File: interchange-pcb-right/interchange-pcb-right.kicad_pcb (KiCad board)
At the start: 2 copper layers, 158 x 104 mm, 139 parts, among them J1 Conn_01x04, J2 Conn_01x04, J3 TRRS_L, J4 TRRS_R, J5 SSD1306, SW1 RotaryEncoder, U1 Seeeduino Xiao rp2040, U2 PCA9555PW, U3 PCA9555PW, U4 ADS1110, U5 SN74AHCT125PWR, U6 TCA4307DGKR

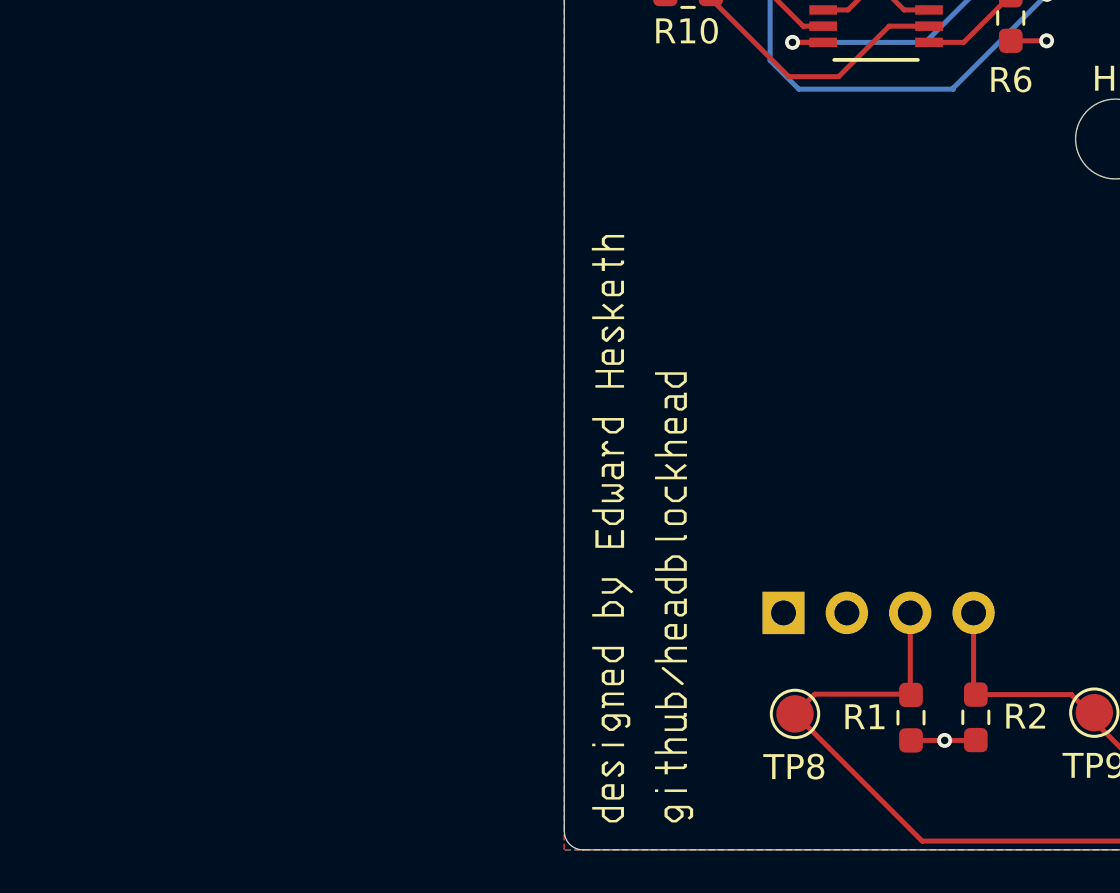
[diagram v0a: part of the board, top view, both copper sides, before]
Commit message: feat: rename right to interchange
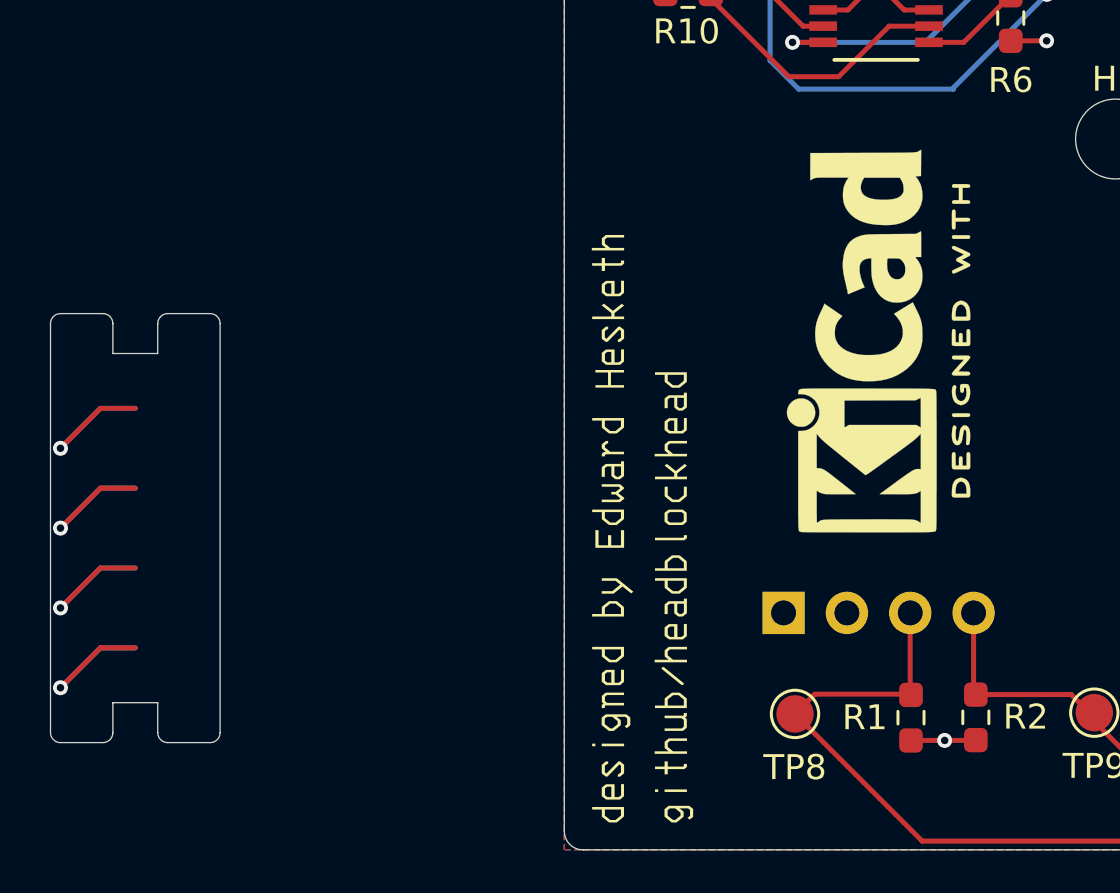
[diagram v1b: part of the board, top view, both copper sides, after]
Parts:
- added REF**: KiCad-Logo2_6mm_SilkScreen, Symbol:KiCad-Logo2_6mm_SilkScreen, F.Cu at (81.9, 129.6)
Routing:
- net (no net): track 0.00 -> 29.3 mm, vias 0 -> 4
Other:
- board size 158 x 104 mm -> 178.6 x 104 mm

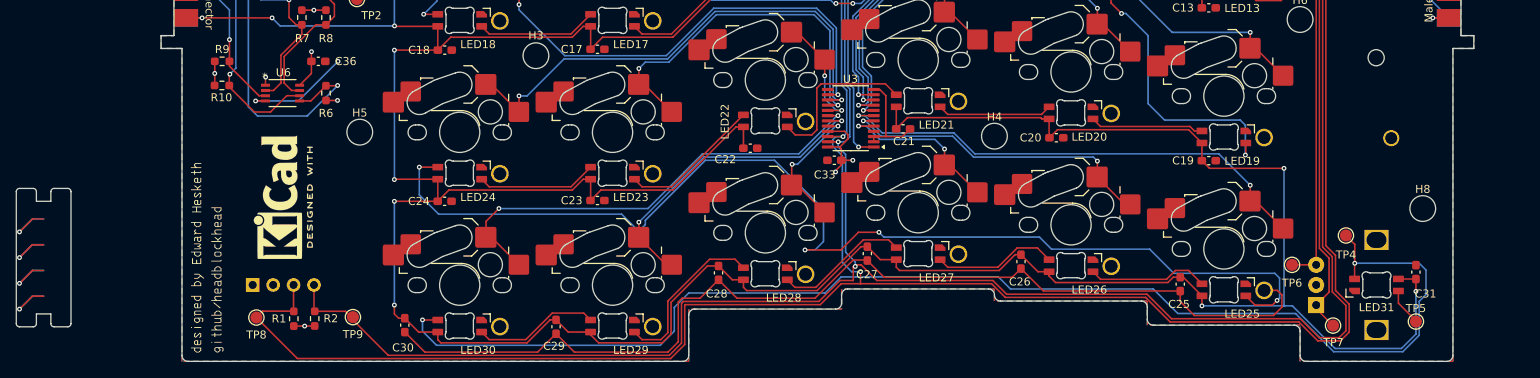
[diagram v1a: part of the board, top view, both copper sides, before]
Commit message: feat: add connectors to pcb-right using snap-off mousebites
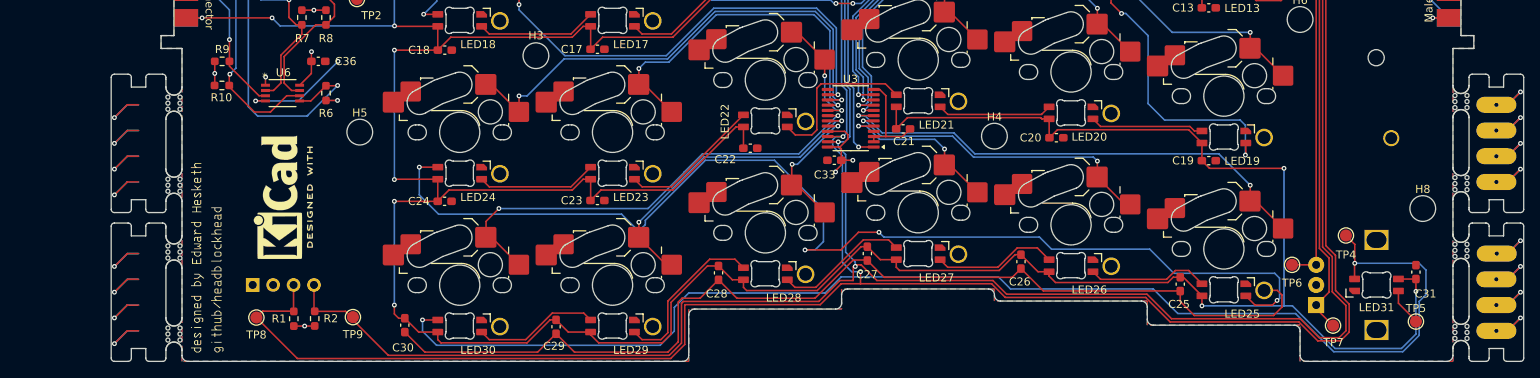
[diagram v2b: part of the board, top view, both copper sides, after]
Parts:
- added REF**: Pogo-0906-0-15-20-76-14-11-0, CustomFootprints:Pogo-0906-0-15-20-76-14-11-0, F.Cu at (233.4, 143.0)
- added REF**: Pogo-0906-0-15-20-76-14-11-0, CustomFootprints:Pogo-0906-0-15-20-76-14-11-0, F.Cu at (233.4, 146.2)
- added REF**: Pogo-0906-0-15-20-76-14-11-0, CustomFootprints:Pogo-0906-0-15-20-76-14-11-0, F.Cu at (233.4, 127.7)
- added REF**: Pogo-0906-0-15-20-76-14-11-0, CustomFootprints:Pogo-0906-0-15-20-76-14-11-0, F.Cu at (233.4, 136.6)
- added REF**: Pogo-0906-0-15-20-76-14-11-0, CustomFootprints:Pogo-0906-0-15-20-76-14-11-0, F.Cu at (233.4, 118.1)
- added REF**: Pogo-0906-0-15-20-76-14-11-0, CustomFootprints:Pogo-0906-0-15-20-76-14-11-0, F.Cu at (233.4, 124.5)
- added REF**: Pogo-0906-0-15-20-76-14-11-0, CustomFootprints:Pogo-0906-0-15-20-76-14-11-0, F.Cu at (233.4, 139.8)
- added REF**: Pogo-0906-0-15-20-76-14-11-0, CustomFootprints:Pogo-0906-0-15-20-76-14-11-0, F.Cu at (233.4, 121.3)
- added mouse-bite-2mm-slot: VAL**, CustomFootprints:mouse-bite-2mm-slot, F.Cu at (229.0, 136.2)
- added mouse-bite-2mm-slot: VAL**, CustomFootprints:mouse-bite-2mm-slot, F.Cu at (69.0, 146.6)
- added mouse-bite-2mm-slot: VAL**, CustomFootprints:mouse-bite-2mm-slot, F.Cu at (69.0, 128.1)
- added mouse-bite-2mm-slot: VAL**, CustomFootprints:mouse-bite-2mm-slot, F.Cu at (69.0, 136.4)
- added mouse-bite-2mm-slot: VAL**, CustomFootprints:mouse-bite-2mm-slot, F.Cu at (229.0, 127.9)
- added mouse-bite-2mm-slot: VAL**, CustomFootprints:mouse-bite-2mm-slot, F.Cu at (69.0, 117.9)
- added mouse-bite-2mm-slot: VAL**, CustomFootprints:mouse-bite-2mm-slot, F.Cu at (229.0, 146.4)
- added mouse-bite-2mm-slot: VAL**, CustomFootprints:mouse-bite-2mm-slot, F.Cu at (229.0, 117.7)
- U5: value SN74AHCT125PWR -> (none)
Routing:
- net (no net): track 29.3 -> 117.2 mm, vias 4 -> 16
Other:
- board size 178.6 x 104 mm -> 175.6 x 104 mm
- board text added: "F"
- board text added: "M"
